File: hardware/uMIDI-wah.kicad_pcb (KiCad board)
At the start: 2 copper layers, 39 parts, among them Q1 BSS138, U1 uA741CDR, X1 9V, X2 uMIDI, X3 Input, X4 Output

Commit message: Continue placement/routing
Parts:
- D1, X2, X3, X4: moved to B.Cu
- moved D1 76.2 mm to (226.0, 130.6)
- moved X2 73.7 mm to (201.5, 145.5), turned to 180 degrees
- moved X1 72.9 mm to (208.8, 125.8), turned to 180 degrees
- moved R11 59.6 mm to (215.2, 134.8), turned to 180 degrees
- moved R12 57.7 mm to (208.8, 134.8), turned to 180 degrees
- moved R14 55.2 mm to (226.0, 133.4), turned to 90 degrees
- moved C1 55.0 mm to (203.8, 126.4), turned to 90 degrees
- moved R2 52.3 mm to (228.0, 133.4), turned to 270 degrees
- moved C13 51.6 mm to (225.0, 139.0), turned to 270 degrees
- moved Q1 49.7 mm to (223.2, 133.4), turned to 90 degrees
- moved R13 46.9 mm to (222.6, 138.4), turned to 0 degrees
- moved C3 46.3 mm to (198.7, 126.7), turned to 270 degrees
- moved R10 45.3 mm to (208.8, 137.2), turned to 180 degrees
- moved D3 43.1 mm to (220.2, 135.0), turned to 90 degrees
- moved C14 42.0 mm to (220.2, 139.0), turned to 270 degrees
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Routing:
- net (no net): track 0.00 -> 109.5 mm
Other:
- board outline added: 55 x 30 mm
- net class Default: clearance 0.2 -> 0.3; trace_width 0.25 -> 0.3
- rule trace_clearance: 0.2 -> 0.3

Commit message: Place and route
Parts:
- added REF**: 1pin, Connect:1pin, F.Cu at (213.2, 138.8)
- added REF**: 1pin, Connect:1pin, F.Cu at (182.5, 147.5)
- added REF**: 1pin, Connect:1pin, F.Cu at (182.5, 130.0)
- C1, C4, C5, C8: footprint Capacitors_SMD:C_0603 -> Capacitors_SMD:C_0805
- R8: value Photores -> LDR 05; footprint Resistors_ThroughHole:Resistor_Horizontal_RM10mm -> Capacitors_Elko_ThroughHole:Elko_vert_20x10mm_RM7.5
- X1: moved to B.Cu
- moved C4 22.3 mm to (191.5, 147.5), turned to 270 degrees
- moved C5 22.2 mm to (189.0, 147.5), turned to 270 degrees
- moved C2 21.5 mm to (208.8, 146.8), turned to 90 degrees
- moved X1 21.0 mm to (212.5, 146.5)
- moved R3 20.8 mm to (186.8, 147.0), turned to 90 degrees
- moved C1 20.6 mm to (206.8, 146.8), turned to 270 degrees
- moved X2 20.0 mm to (220.2, 138.8), turned to 270 degrees
- moved C3 16.2 mm to (184.4, 134.2), turned to 180 degrees
- moved D1 15.8 mm to (210.2, 131.8)
- moved R5 14.1 mm to (183.0, 144.0), turned to 180 degrees
- moved C8 14.0 mm to (186.5, 144.0), turned to 180 degrees
- moved R4 14.0 mm to (194.5, 146.2), turned to 0 degrees
- moved R14 13.8 mm to (212.2, 134.8)
- moved R2 13.8 mm to (214.2, 134.8)
- moved Q1 13.8 mm to (209.5, 134.8)
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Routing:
- net GND: track 11.6 -> 156.4 mm
- net (no net): track 109.5 -> 0.00 mm
- net +9V: track 13.4 -> 47.5 mm
- net Net-(D2-Pad2): track 0.00 -> 21.9 mm
- net /True bypass/Ctrl: track 0.00 -> 8.86 mm
- net /PWM: track 0.00 -> 8.46 mm
- net Net-(C11-Pad1): track 0.00 -> 6.26 mm
- net /True bypass/relais_p: track 0.00 -> 5.78 mm
- net /True bypass/FX_Send: track 0.00 -> 5.43 mm
- net /True bypass/FX_Return: track 0.00 -> 5.35 mm
- net /True bypass/bypass: track 0.00 -> 5.10 mm
- net /True bypass/relais_n: track 0.00 -> 4.99 mm
- net /True bypass/Loop_Out: track 0.00 -> 4.46 mm
- net /True bypass/Loop_In: track 0.00 -> 4.46 mm
- net Net-(C12-Pad1): track 0.00 -> 3.73 mm
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- added copper zone on F.Cu, net GND
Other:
- board size 55 x 30 mm -> 45 x 22.5 mm

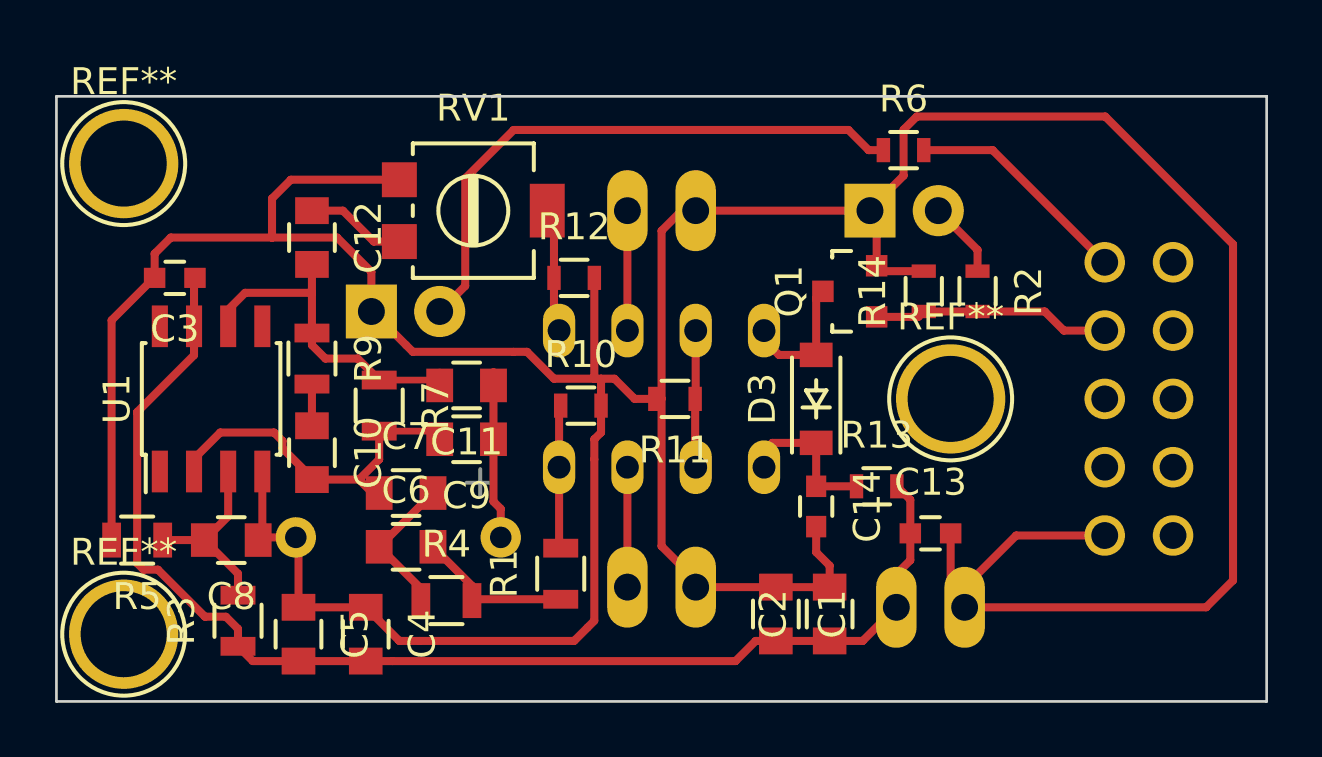
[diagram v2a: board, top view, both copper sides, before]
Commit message: Add filter circuit to the pwm led
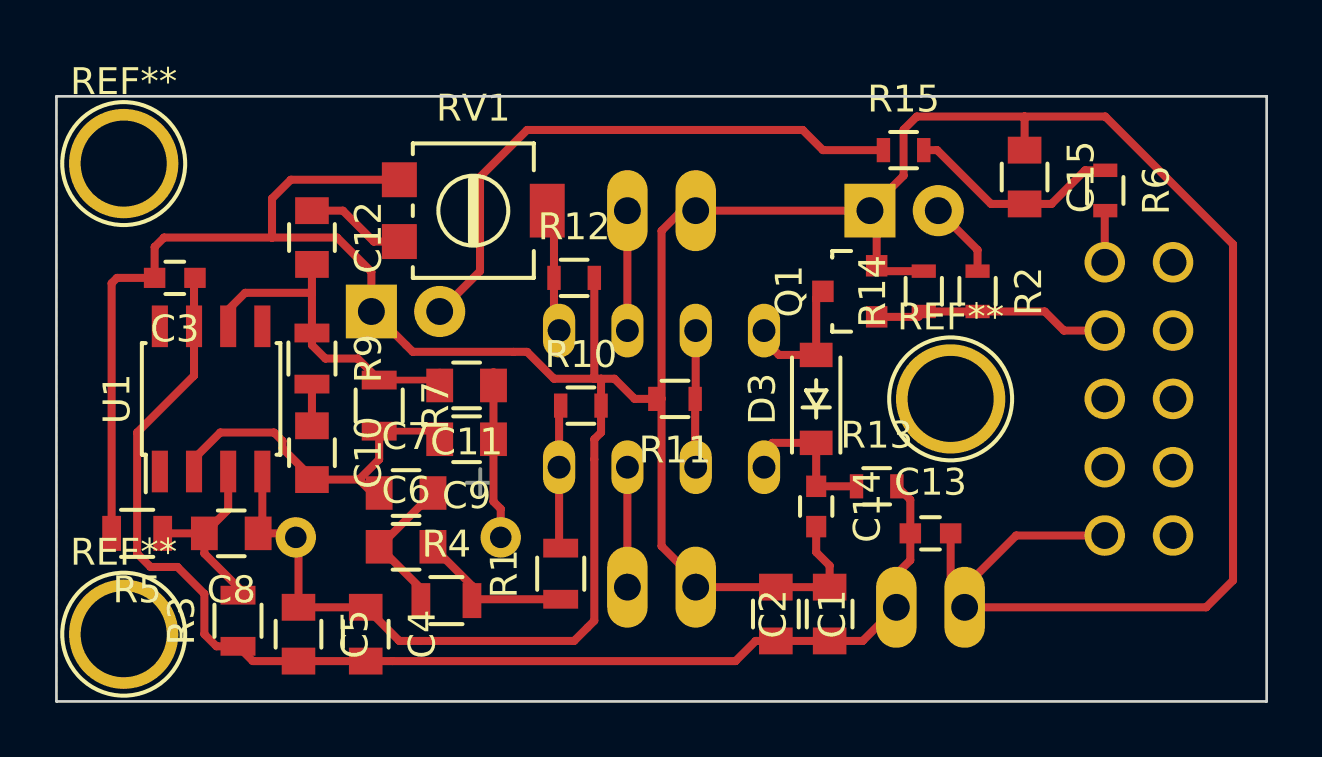
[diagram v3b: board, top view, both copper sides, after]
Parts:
- added C15: 10u, Capacitors_SMD:C_0805, F.Cu at (216.0, 130.5)
- added R15: 39, Resistors_SMD:R_0603, F.Cu at (211.5, 129.5)
- R6: value 82 -> 39
- moved R6 7.65 mm to (219.0, 131.0), turned to 270 degrees
- moved C8 0.25 mm to (186.5, 143.8)
- moved R5 0.25 mm to (183.0, 143.8)
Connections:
- R6 pad 1: Net-(D2-Pad2) -> Net-(C15-Pad2)
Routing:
- net Net-(C15-Pad2): track 0.00 -> 8.10 mm
- net /PWM: track 8.46 -> 1.93 mm
- net GND: track 156.4 -> 158.0 mm

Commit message: Replace opamp uA741 by TL071
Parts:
- U1: value uA741CDR -> TL071CPSR
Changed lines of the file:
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@@
       (effects (font (size 1 1) (thickness 0.15)))
     )
-    (fp_text value uA741CDR (at 0 3.5 90) (layer F.Fab)
+    (fp_text value TL071CPSR (at 0 3.5 90) (layer F.Fab)
       (effects (font (size 1 1) (thickness 0.15)))
     )

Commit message: DRC clean
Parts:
- moved REF** 1.50 mm to (182.5, 128.5)
- moved C1 1.00 mm to (206.8, 145.8)
- moved C10 1.00 mm to (189.5, 139.8)
- moved C11 1.00 mm to (195.2, 137.2)
- moved C12 1.00 mm to (189.5, 131.8)
- moved C13 1.00 mm to (212.5, 142.8)
- moved C14 1.00 mm to (208.2, 141.8)
- moved C15 1.00 mm to (216.0, 129.5)
- moved C2 1.00 mm to (208.8, 145.8)
- moved C3 1.00 mm to (184.4, 133.2)
- moved C4 1.00 mm to (191.5, 146.5)
- moved C5 1.00 mm to (189.0, 146.5)
- moved C6 1.00 mm to (193.0, 143.2)
- moved C7 1.00 mm to (193.0, 141.2)
- moved C8 1.00 mm to (186.5, 142.8)
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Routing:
- net Net-(C11-Pad1): track 6.26 -> 5.76 mm
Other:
- board size 45 x 22.5 mm -> 45 x 24 mm
- rule trace_min: 0.2 -> 0.3

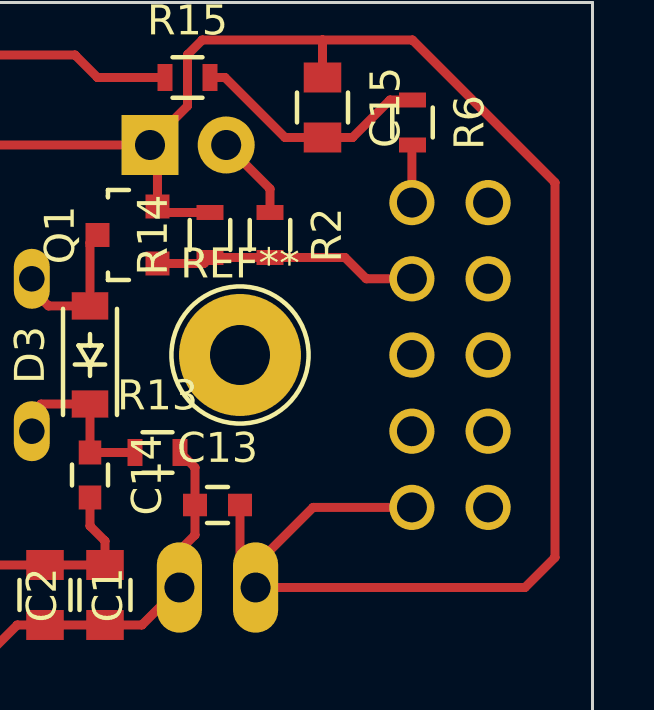
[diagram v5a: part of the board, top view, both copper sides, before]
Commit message: Increase pad size of ribbon connector
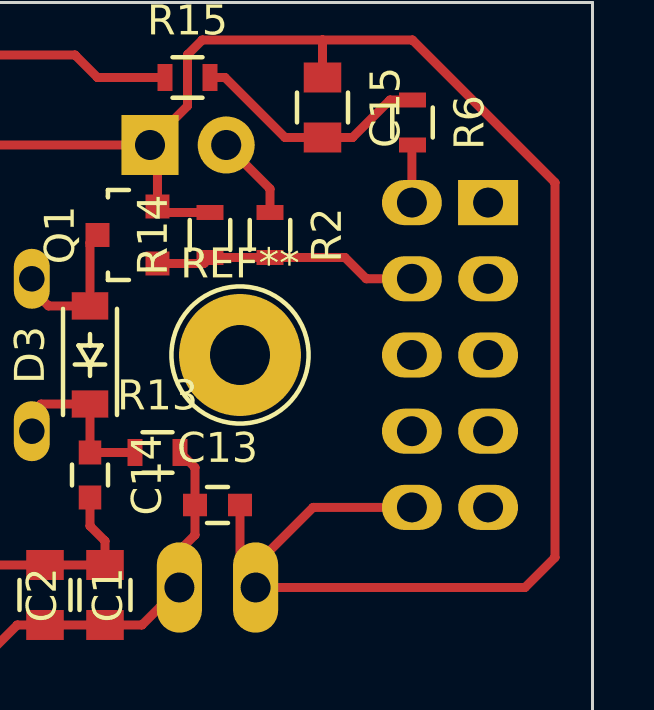
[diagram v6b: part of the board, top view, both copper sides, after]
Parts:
- X2: footprint Connect:VASCH5x2 -> uMIDI-wah:VASCH5x2_diy-pcb
